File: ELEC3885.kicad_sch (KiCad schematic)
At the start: 17 parts, among them U2 SGTL5000XNLA3, U3 AP7313

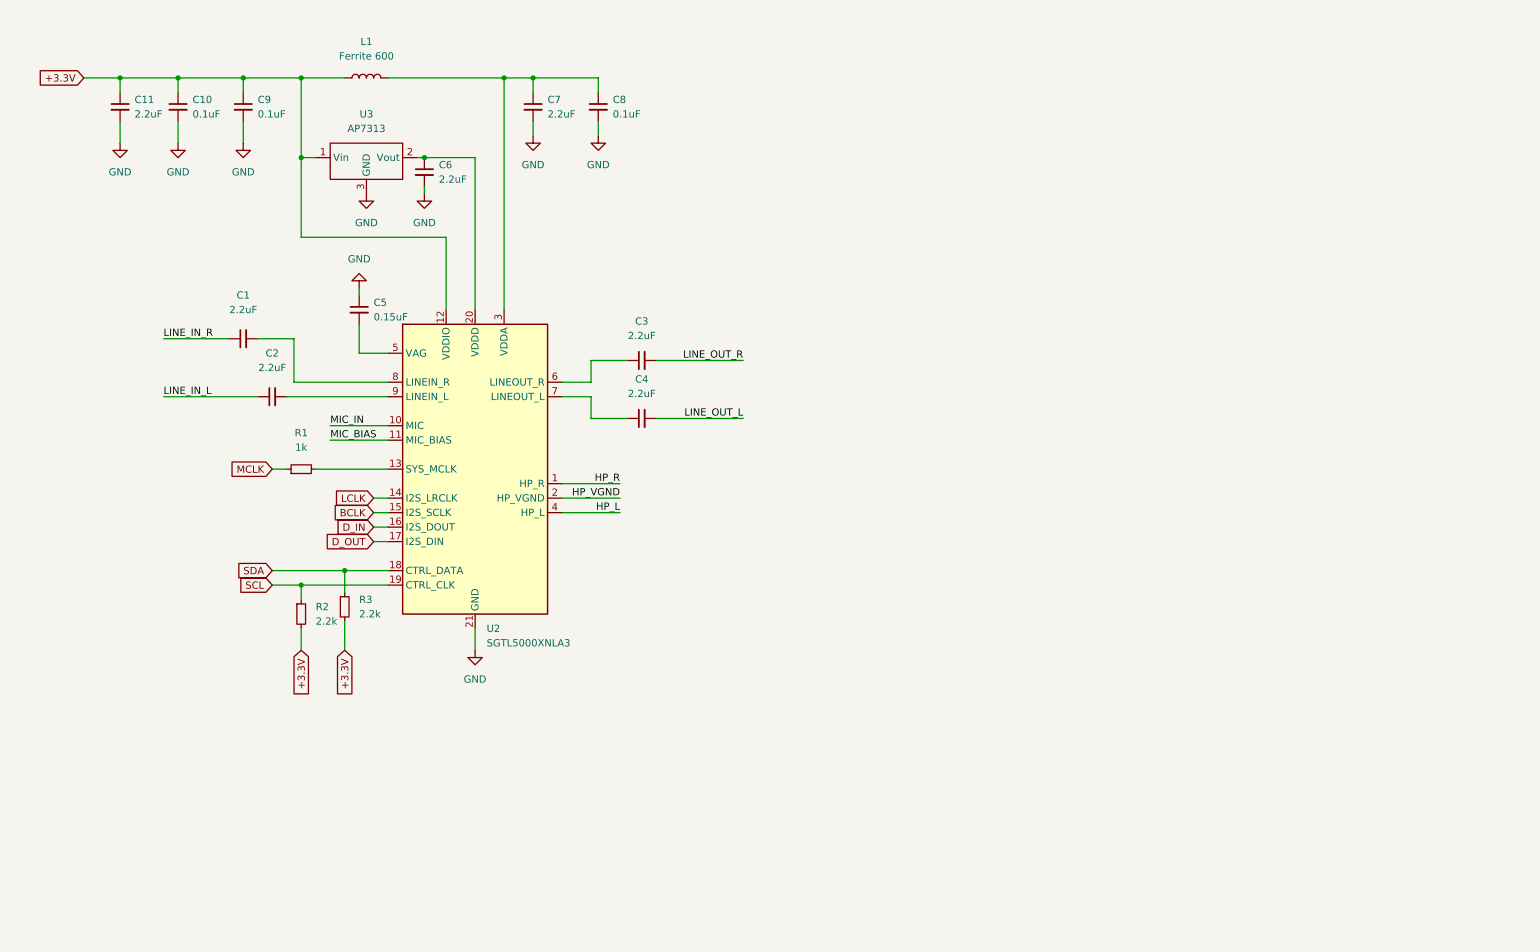
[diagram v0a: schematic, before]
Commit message: Audio connections and internal mic added
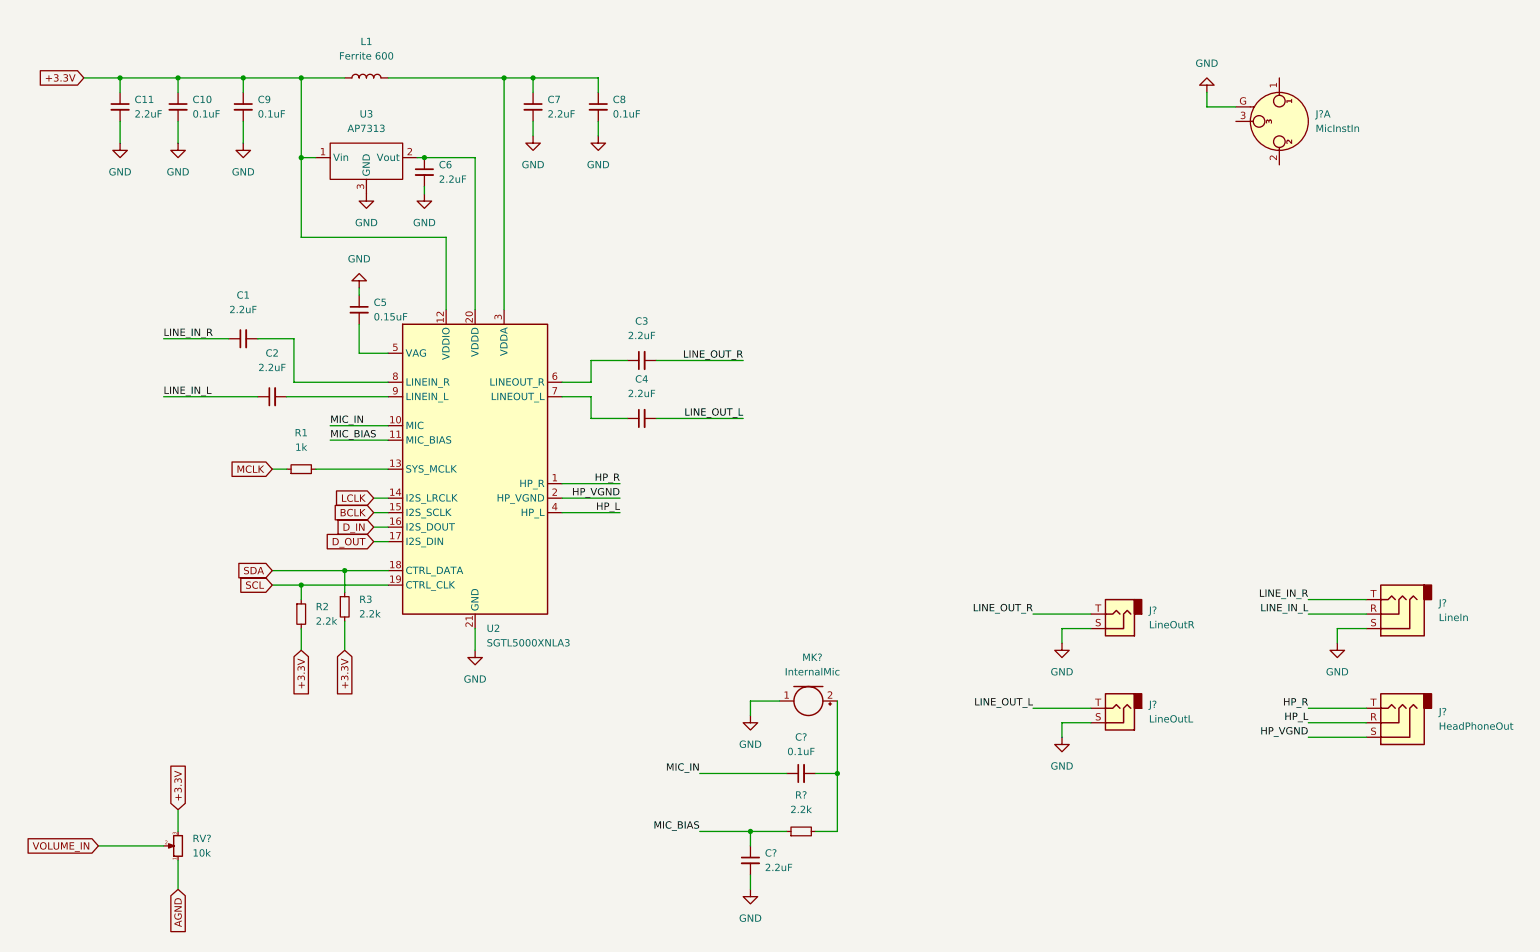
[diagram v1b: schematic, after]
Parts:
- added C?: 0.1uF, symbol Device:C_Small
- added C?: 2.2uF, symbol Device:C_Small
- added J?: MicInstIn, symbol Connector:XLR3_AudioJack3_Combo_Ground
- added J?: LineOutL, symbol Connector:AudioJack2
- added J?: HeadPhoneOut, symbol Connector:AudioJack3
- added J?: LineOutR, symbol Connector:AudioJack2
- added J?: LineIn, symbol Connector:AudioJack3
- added MK?: InternalMic, symbol Device:Microphone
- added R?: 2.2k, symbol Device:R_Small
- added RV?: 10k, symbol Device:R_Potentiometer_Small
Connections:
- net +3.3V: now also RV?.3
- net GND: now also C?.2, J?.G, J?.S, J?.S, J?.S, MK?.1 (-)
- net HP_L: now also J?.R
- net HP_R: now also J?.T
- net HP_VGND: now also J?.S
- net LINE_IN_L: now also J?.R
- net LINE_IN_R: now also J?.T
- net LINE_OUT_L: now also J?.T
- net LINE_OUT_R: now also J?.T
- net MIC_BIAS: now also C?.1, R?.1
- net MIC_IN: now also C?.1
- new net: C?.2, MK?.2 (+), R?.2
- new net AGND: RV?.1
- new net VOLUME_IN: RV?.2

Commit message: Hierarchical sheets setup
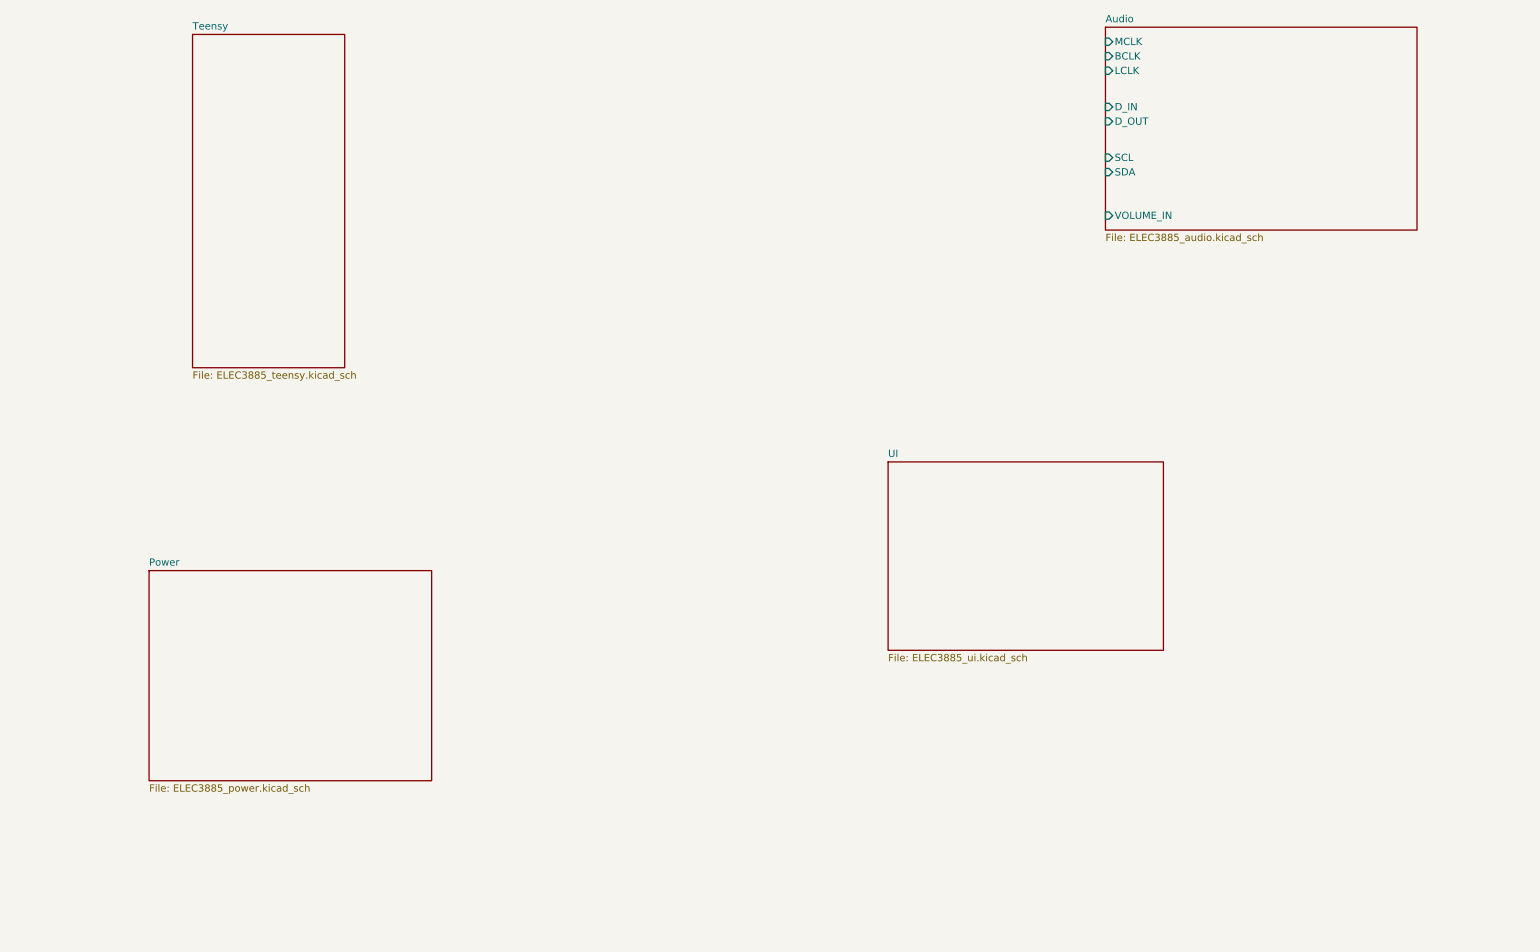
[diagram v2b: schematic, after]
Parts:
- removed C1, C11, C2, C3, C4, C6, C7, C?: 2.2uF, symbol Device:C_Small
- removed C10, C8, C9, C?: 0.1uF, symbol Device:C_Small
- removed C5: 0.15uF, symbol Device:C_Small
- removed J?: MicInstIn, symbol Connector:XLR3_AudioJack3_Combo_Ground
- removed J?: LineOutL, symbol Connector:AudioJack2
- removed J?: HeadPhoneOut, symbol Connector:AudioJack3
- removed J?: LineOutR, symbol Connector:AudioJack2
- removed J?: LineIn, symbol Connector:AudioJack3
- removed L1: Ferrite 600, symbol Device:L
- removed MK?: InternalMic, symbol Device:Microphone
- removed R1: 1k, symbol Device:R_Small
- removed R2, R3, R?: 2.2k, symbol Device:R_Small
- removed RV?: 10k, symbol Device:R_Potentiometer_Small
- removed U2: SGTL5000XNLA3, Package_DFN_QFN:QFN-20-1EP_3x3mm_P0.4mm_EP1.65x1.65mm, symbol Audio:SGTL5000XNLA3
- removed U3: AP7313, symbol Luke_Library:AP7313
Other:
- added sheet Audio (ELEC3885_audio.kicad_sch)
- added sheet Power (ELEC3885_power.kicad_sch)
- added sheet Teensy (ELEC3885_teensy.kicad_sch)
- added sheet UI (ELEC3885_ui.kicad_sch)

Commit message: Schematic work
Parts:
- added H1, H2, H3, H4: MountingHole, MountingHole:MountingHole_3.2mm_M3, symbol Mechanical:MountingHole
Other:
- sheet Audio ports: added VOLUME_CONTROL; removed VOLUME_IN
- sheet Teensy ports: added BCLK, D_IN, D_OUT, LRCLK, MCLK, SCL, SDA, VOLUME_CONTROL; removed none

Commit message: Initial schematic complete
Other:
- sheet Teensy ports: added BUTTON_0, BUTTON_1, BUTTON_2, BUTTON_3; removed none
- sheet UI ports: added BUTTON_0, BUTTON_1, BUTTON_2, BUTTON_3; removed none
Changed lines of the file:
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@@
+    (stroke (width 0) (type default) (color 0 0 0 0))
+  )
+  (wire (pts (xy 132.08 88.9) (xy 132.08 120.65))
     (stroke (width 0) (type default) (color 0 0 0 0))
   )
@@
     (stroke (width 0) (type default) (color 0 0 0 0))
   )
+  (wire (pts (xy 139.7 81.28) (xy 139.7 113.03))
+    (stroke (width 0) (type default) (color 0 0 0 0))
+  )
   (wire (pts (xy 77.47 41.91) (xy 102.87 41.91))
     (stroke (width 0) (type default) (color 0 0 0 0))
   )
+  (wire (pts (xy 77.47 83.82) (xy 137.16 83.82))
+    (stroke (width 0) (type default) (color 0 0 0 0))
+  )
+  (wire (pts (xy 134.62 86.36) (xy 134.62 118.11))
+    (stroke (width 0) (type default) (color 0 0 0 0))
+  )
+  (wire (pts (xy 77.47 88.9) (xy 132.08 88.9))
+    (stroke (width 0) (type default) (color 0 0 0 0))
+  )
   (wire (pts (xy 77.47 54.61) (xy 102.87 54.61))
     (stroke (width 0) (type default) (color 0 0 0 0))
@@
     (stroke (width 0) (type default) (color 0 0 0 0))
   )
+  (wire (pts (xy 137.16 115.57) (xy 172.72 115.57))
+    (stroke (width 0) (type default) (color 0 0 0 0))
+  )
+  (wire (pts (xy 137.16 83.82) (xy 137.16 115.57))
+    (stroke (width 0) (type default) (color 0 0 0 0))
+  )
   (wire (pts (xy 77.47 39.37) (xy 102.87 39.37))
     (stroke (width 0) (type default) (color 0 0 0 0))
   )
+  (wire (pts (xy 77.47 86.36) (xy 134.62 86.36))
+    (stroke (width 0) (type default) (color 0 0 0 0))
+  )
+  (wire (pts (xy 132.08 120.65) (xy 172.72 120.65))
+    (stroke (width 0) (type default) (color 0 0 0 0))
+  )
+  (wire (pts (xy 77.47 81.28) (xy 139.7 81.28))
+    (stroke (width 0) (type default) (color 0 0 0 0))
+  )
+  (wire (pts (xy 139.7 113.03) (xy 172.72 113.03))
+    (stroke (width 0) (type default) (color 0 0 0 0))
+  )
   (wire (pts (xy 77.47 52.07) (xy 102.87 52.07))
+    (stroke (width 0) (type default) (color 0 0 0 0))
+  )
+  (wire (pts (xy 134.62 118.11) (xy 172.72 118.11))
     (stroke (width 0) (type default) (color 0 0 0 0))
   )
@@
       (effects (font (size 1.27 1.27)) (justify right))
     )
+    (pin "BUTTON_0" output (at 77.47 81.28 0)
+      (effects (font (size 1.27 1.27)) (justify right))
+    )
+    (pin "BUTTON_3" output (at 77.47 88.9 0)
+      (effects (font (size 1.27 1.27)) (justify right))
+    )
+    (pin "BUTTON_1" output (at 77.47 83.82 0)
+      (effects (font (size 1.27 1.27)) (justify right))
+    )
+    (pin "BUTTON_2" output (at 77.47 86.36 0)
+      (effects (font (size 1.27 1.27)) (justify right))
+    )
   )
   (sheet (at 172.72 109.22) (size 48.26 33.02) (fields_autoplaced)
@@
     (property "Sheet file" "ELEC3885_ui.kicad_sch" (id 1) (at 172.72 142.8246 0)
       (effects (font (size 1.27 1.27)) (justify left top))
+    )
+    (pin "BUTTON_3" input (at 172.72 120.65 180)
+      (effects (font (size 1.27 1.27)) (justify left))
+    )
+    (pin "BUTTON_0" input (at 172.72 113.03 180)
+      (effects (font (size 1.27 1.27)) (justify left))
+    )
+    (pin "BUTTON_2" input (at 172.72 118.11 180)
+      (effects (font (size 1.27 1.27)) (justify left))
+    )
+    (pin "BUTTON_1" input (at 172.72 115.57 180)
+      (effects (font (size 1.27 1.27)) (justify left))
     )
   )
@@
   )
   (symbol_instances
-    (path "/ffd175d1-912a-4224-be1e-a8198680f46b/f17b27f4-2e76-4095-9aeb-4abad9f5f10c"
-      (reference "#PWR01") (unit 1) (value "GND") (footprint "")
-    )
     (path "/ffd175d1-912a-4224-be1e-a8198680f46b/4d12293e-9aac-483b-8ba9-b6c8aa32ac7f"
       (reference "#PWR02") (unit 1) (value "GND") (footprint "")
@@
       (reference "#PWR017") (unit 1) (value "GND") (footprint "")
     )
+    (path "/ffd175d1-912a-4224-be1e-a8198680f46b/be6339c8-eb8d-4617-8a40-c1211ef569be"
+      (reference "#PWR0101") (unit 1) (value "GND") (footprint "")
+    )
+    (path "/ffd175d1-912a-4224-be1e-a8198680f46b/04034e68-0810-40df-850a-9d6c6ecc1ea0"
+      (reference "#PWR0102") (unit 1) (value "GND") (footprint "")
+    )
+    (path "/ffd175d1-912a-4224-be1e-a8198680f46b/06d02ba4-1e3a-458a-8edf-a18e45639ac4"
+      (reference "#PWR0103") (unit 1) (value "GND") (footprint "")
+    )
+    (path "/edb4d620-a826-41be-bd87-be038303d2ba/bae38154-fc79-48f2-95f9-137bbc516bbe"
+      (reference "#PWR0104") (unit 1) (value "GND") (footprint "")
+    )
     (path "/ffd175d1-912a-4224-be1e-a8198680f46b/14024c61-79e8-40dc-9057-37cc4ebba99b"
       (reference "C1") (unit 1) (value "10uF") (footprint "Capacitor_SMD:C_0603_1608Metric")
@@
       (reference "J7") (unit 1) (value "Conn_01x24_Female") (footprint "Connector_PinSocket_2.54mm:PinSocket_1x24_P2.54mm_Vertical")
     )
+    (path "/ffd175d1-912a-4224-be1e-a8198680f46b/8a5e8b89-c319-442f-a653-f87e9da317ff"
+      (reference "J8") (unit 1) (value "Conn_01x06_Female") (footprint "Connector_PinSocket_2.54mm:PinSocket_1x06_P2.54mm_Vertical")
+    )
+    (path "/ffd175d1-912a-4224-be1e-a8198680f46b/3ee37db4-a39b-4005-b2dd-8f340e39579a"
+      (reference "J9") (unit 1) (value "Conn_01x05_Female") (footprint "Connector_PinSocket_2.54mm:PinSocket_1x05_P2.54mm_Vertical")
+    )
     (path "/ffd175d1-912a-4224-be1e-a8198680f46b/7161c77f-7beb-42e2-87ce-84dbaf047b7a"
       (reference "MK1") (unit 1) (value "InternalMic") (footprint "Connector_PinSocket_2.54mm:PinSocket_1x02_P2.54mm_Vertical")
@@
       (reference "RV1") (unit 1) (value "10k") (footprint "Potentiometer_THT:Potentiometer_Alpha_RD901F-40-00D_Single_Vertical")
     )
+    (path "/edb4d620-a826-41be-bd87-be038303d2ba/f2e46452-c864-4715-bf5e-3c162fa31679"
+      (reference "SW1") (unit 1) (value "SW_Push") (footprint "Button_Switch_SMD:SW_Push_1P1T_NO_6x6mm_H9.5mm")
+    )
+    (path "/edb4d620-a826-41be-bd87-be038303d2ba/3979b95e-da15-4b69-96e7-9492ef78b3b7"
+      (reference "SW2") (unit 1) (value "SW_Push") (footprint "Button_Switch_SMD:SW_Push_1P1T_NO_6x6mm_H9.5mm")
+    )
+    (path "/edb4d620-a826-41be-bd87-be038303d2ba/63e84925-9fbf-4be0-a474-0422f7436c46"
+      (reference "SW3") (unit 1) (value "SW_Push") (footprint "Button_Switch_SMD:SW_Push_1P1T_NO_6x6mm_H9.5mm")
+    )
+    (path "/edb4d620-a826-41be-bd87-be038303d2ba/56908d31-e0ae-4ae5-9e55-9383d2983eb0"
+      (reference "SW4") (unit 1) (value "SW_Push") (footprint "Button_Switch_SMD:SW_Push_1P1T_NO_6x6mm_H9.5mm")
+    )
     (path "/ffd175d1-912a-4224-be1e-a8198680f46b/6eb9e700-3d11-4035-bf7b-da800e96c463"
